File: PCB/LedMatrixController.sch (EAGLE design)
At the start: 31 parts, among them IC2 74LS595D, X1 MINI-USB-32005-201

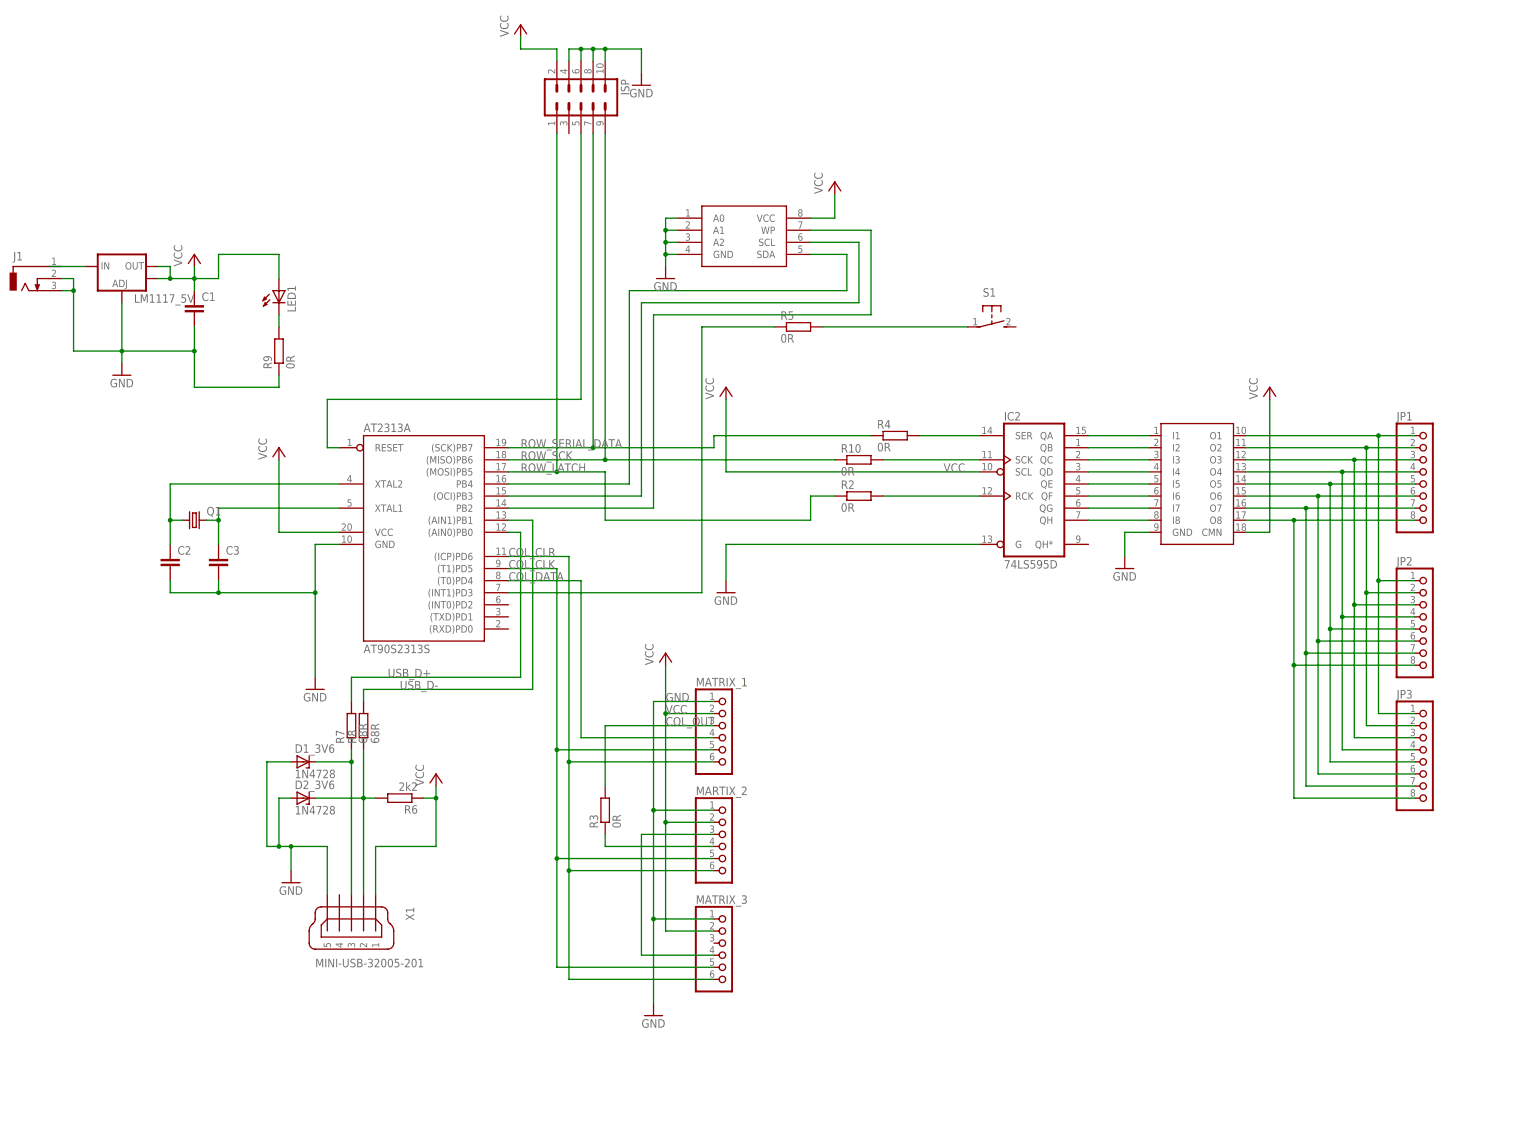
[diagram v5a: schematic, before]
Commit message: Finished first version of the led matrix controller pcb
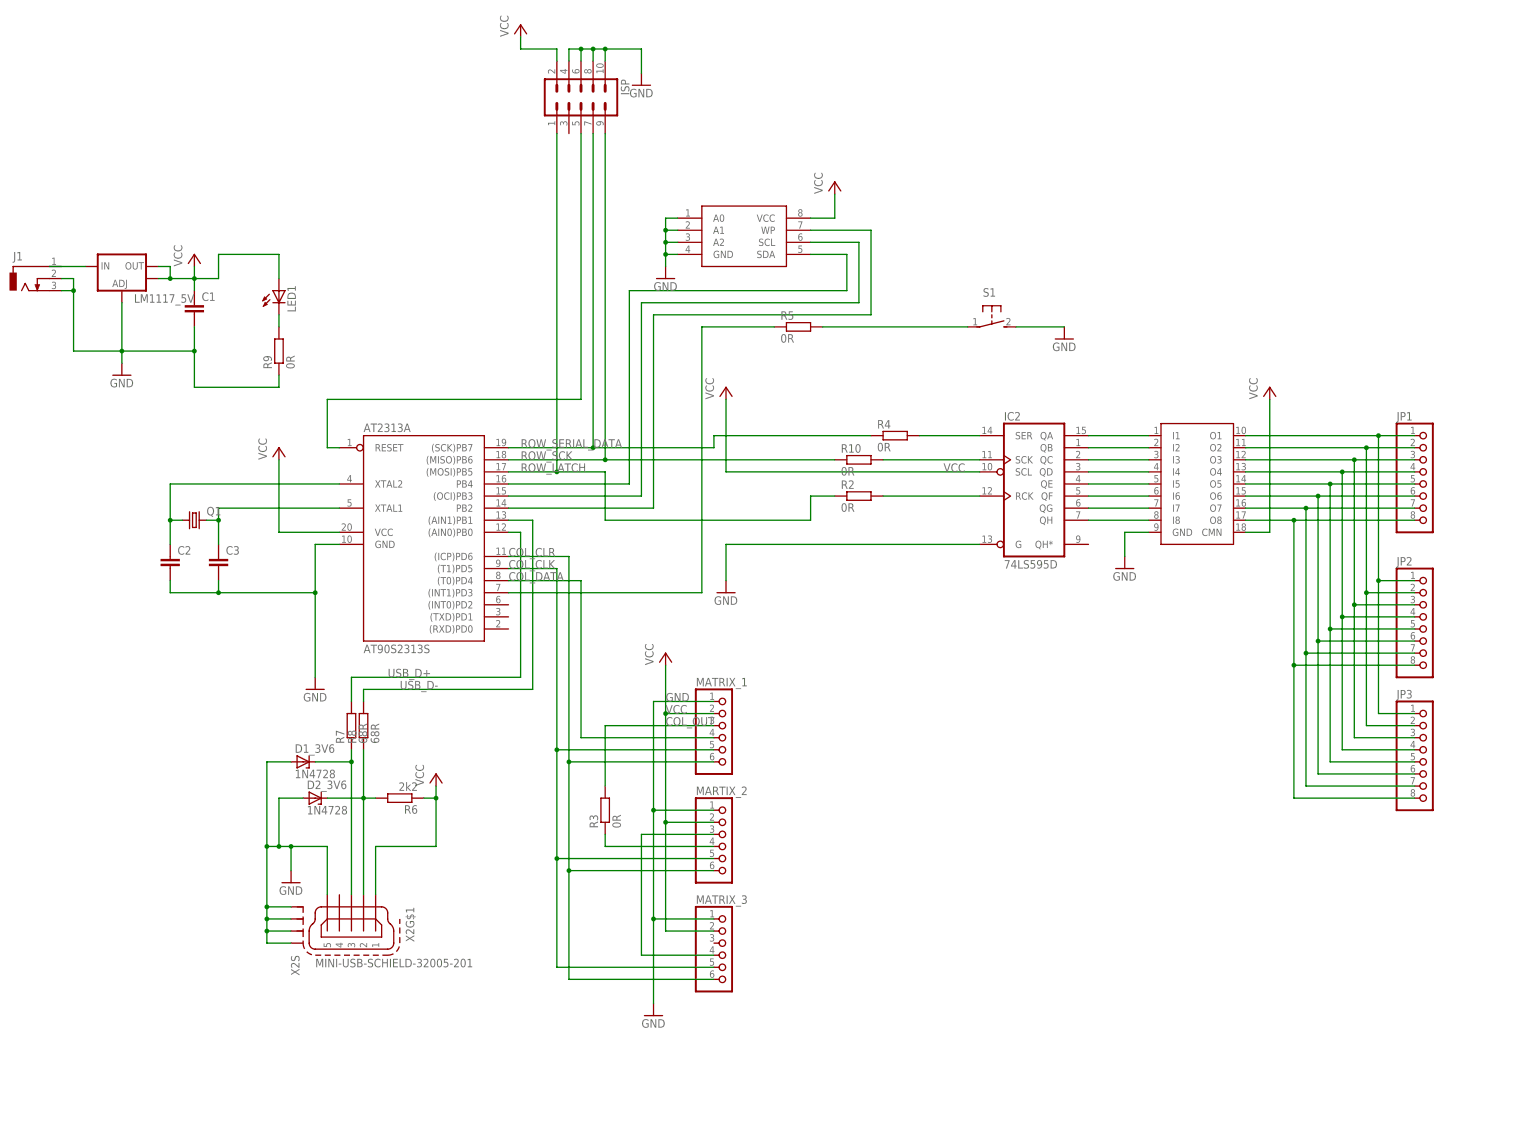
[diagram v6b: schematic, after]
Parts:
- removed X1: MINI-USB-32005-201, con-cypressindustries:MINI-USB-32005-201
- added X2: MINI-USB-SCHIELD-32005-201, con-cypressindustries:MINI-USB-SCHIELD-32005-201
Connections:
- net GND: now also S1.S, X2G$1.5, X2S.S1, X2S.S2, X2S.S3, X2S.S4; no longer X1.5
- net USB_DATA+: now also X2G$1.3; no longer X1.3
- net USB_DATA-: now also X2G$1.2; no longer X1.2
- net VCC: now also X2G$1.1; no longer X1.1
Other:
- moved on the sheet: D2_3V6
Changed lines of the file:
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@@
 <layers>
 <layer number="1" name="Top" color="4" fill="1" visible="no" active="no"/>
-<layer number="16" name="Bottom" color="1" fill="1" visible="no" active="no"/>
+<layer number="16" name="Bottom" color="11" fill="1" visible="no" active="no"/>
 <layer number="17" name="Pads" color="2" fill="1" visible="no" active="no"/>
 <layer number="18" name="Vias" color="2" fill="1" visible="no" active="no"/>
-<layer number="19" name="Unrouted" color="6" fill="1" visible="no" active="no"/>
+<layer number="19" name="Unrouted" color="14" fill="1" visible="no" active="no"/>
 <layer number="20" name="Dimension" color="15" fill="1" visible="no" active="no"/>
 <layer number="21" name="tPlace" color="7" fill="1" visible="no" active="no"/>
@@
 <part name="P+7" library="supply1" deviceset="VCC" device=""/>
 <part name="R5" library="resistor" deviceset="R-EU_" device="R1206" value="0R"/>
-<part name="X1" library="con-cypressindustries" deviceset="MINI-USB-" device="32005-201"/>
 <part name="GND8" library="supply1" deviceset="GND" device=""/>
 <part name="P+8" library="supply1" deviceset="VCC" device=""/>
@@
 <part name="R4" library="resistor" deviceset="R-EU_" device="R1206" value="0R"/>
 <part name="R10" library="resistor" deviceset="R-EU_" device="R1206" value="0R"/>
+<part name="X2" library="con-cypressindustries" deviceset="MINI-USB-SCHIELD-" device="32005-201"/>
+<part name="GND9" library="supply1" deviceset="GND" device=""/>
 </parts>
 <sheets>
@@
 <instance part="P+7" gate="VCC" x="223.52" y="76.2"/>
 <instance part="R5" gate="G$1" x="124.46" y="88.9"/>
-<instance part="X1" gate="G$1" x="30.48" y="-35.56" rot="R270"/>
 <instance part="GND8" gate="1" x="17.78" y="-27.94"/>
 <instance part="P+8" gate="VCC" x="48.26" y="-5.08"/>
@@
 <instance part="R8" gate="G$1" x="33.02" y="5.08" rot="R90"/>
 <instance part="D1_3V6" gate="1" x="20.32" y="-2.54"/>
-<instance part="D2_3V6" gate="1" x="20.32" y="-10.16"/>
+<instance part="D2_3V6" gate="1" x="22.86" y="-10.16"/>
 <instance part="LED1" gate="G$1" x="15.24" y="96.52"/>
 <instance part="R9" gate="G$1" x="15.24" y="83.82" rot="R90"/>
 <instance part="R4" gate="G$1" x="144.78" y="66.04"/>
 <instance part="R10" gate="G$1" x="137.16" y="60.96"/>
+<instance part="X2" gate="G$1" x="30.48" y="-35.56" rot="R270"/>
+<instance part="X2" gate="S" x="20.32" y="-35.56" rot="R270"/>
+<instance part="GND9" gate="1" x="180.34" y="86.36"/>
 </instances>
 <busses>
@@
 <wire x1="17.78" y1="-25.4" x2="17.78" y2="-20.32" width="0.1524" layer="91"/>
 <wire x1="17.78" y1="-20.32" x2="25.4" y2="-20.32" width="0.1524" layer="91"/>
-<pinref part="X1" gate="G$1" pin="5"/>
 <wire x1="25.4" y1="-20.32" x2="25.4" y2="-30.48" width="0.1524" layer="91"/>
 <pinref part="D2_3V6" gate="1" pin="A"/>
-<wire x1="17.78" y1="-10.16" x2="15.24" y2="-10.16" width="0.1524" layer="91"/>
+<wire x1="20.32" y1="-10.16" x2="15.24" y2="-10.16" width="0.1524" layer="91"/>
 <wire x1="15.24" y1="-10.16" x2="15.24" y2="-20.32" width="0.1524" layer="91"/>
 <wire x1="15.24" y1="-20.32" x2="17.78" y2="-20.32" width="0.1524" layer="91"/>
@@
 <junction x="17.78" y="-20.32"/>
 <junction x="15.24" y="-20.32"/>
+<pinref part="X2" gate="G$1" pin="5"/>
+<pinref part="X2" gate="S" pin="S1"/>
+<wire x1="17.78" y1="-33.02" x2="12.7" y2="-33.02" width="0.1524" layer="91"/>
+<wire x1="12.7" y1="-33.02" x2="12.7" y2="-20.32" width="0.1524" layer="91"/>
+<wire x1="12.7" y1="-33.02" x2="12.7" y2="-35.56" width="0.1524" layer="91"/>
+<pinref part="X2" gate="S" pin="S2"/>
+<wire x1="17.78" y1="-35.56" x2="12.7" y2="-35.56" width="0.1524" layer="91"/>
+<wire x1="12.7" y1="-35.56" x2="12.7" y2="-38.1" width="0.1524" layer="91"/>
+<pinref part="X2" gate="S" pin="S3"/>
+<wire x1="17.78" y1="-38.1" x2="12.7" y2="-38.1" width="0.1524" layer="91"/>
+<wire x1="12.7" y1="-38.1" x2="12.7" y2="-40.64" width="0.1524" layer="91"/>
+<pinref part="X2" gate="S" pin="S4"/>
+<wire x1="12.7" y1="-40.64" x2="17.78" y2="-40.64" width="0.1524" layer="91"/>
+<junction x="12.7" y="-38.1"/>
+<junction x="12.7" y="-35.56"/>
+<junction x="12.7" y="-33.02"/>
+<junction x="12.7" y="-20.32"/>
+</segment>
+<segment>
+<pinref part="S1" gate="1" pin="S"/>
+<pinref part="GND9" gate="1" pin="GND"/>
+<wire x1="170.18" y1="88.9" x2="180.34" y2="88.9" width="0.1524" layer="91"/>
 </segment>
 </net>
@@
 </segment>
 <segment>
-<pinref part="X1" gate="G$1" pin="1"/>
 <wire x1="35.56" y1="-30.48" x2="35.56" y2="-20.32" width="0.1524" layer="91"/>
 <wire x1="35.56" y1="-20.32" x2="48.26" y2="-20.32" width="0.1524" layer="91"/>
@@
 <wire x1="45.72" y1="-10.16" x2="48.26" y2="-10.16" width="0.1524" layer="91"/>
 <junction x="48.26" y="-10.16"/>
+<pinref part="X2" gate="G$1" pin="1"/>
 </segment>
 </net>
@@
 <net name="USB_DATA+" class="0">
 <segment>
-<pinref part="X1" gate="G$1" pin="3"/>
 <wire x1="30.48" y1="-30.48" x2="30.48" y2="-2.54" width="0.1524" layer="91"/>
 <pinref part="R7" gate="G$1" pin="1"/>
@@
 <wire x1="22.86" y1="-2.54" x2="30.48" y2="-2.54" width="0.1524" layer="91"/>
 <junction x="30.48" y="-2.54"/>
+<pinref part="X2" gate="G$1" pin="3"/>
 </segment>
 </net>
 <net name="USB_DATA-" class="0">
 <segment>
-<pinref part="X1" gate="G$1" pin="2"/>
 <wire x1="33.02" y1="-30.48" x2="33.02" y2="-10.16" width="0.1524" layer="91"/>
 <pinref part="R8" gate="G$1" pin="1"/>
@@
 <junction x="33.02" y="-10.16"/>
 <pinref part="D2_3V6" gate="1" pin="C"/>
-<wire x1="22.86" y1="-10.16" x2="33.02" y2="-10.16" width="0.1524" layer="91"/>
-</segment>
-</net>
+<wire x1="25.4" y1="-10.16" x2="33.02" y2="-10.16" width="0.1524" layer="91"/>
+<pinref part="X2" gate="G$1" pin="2"/>
+</segment>
+</net>

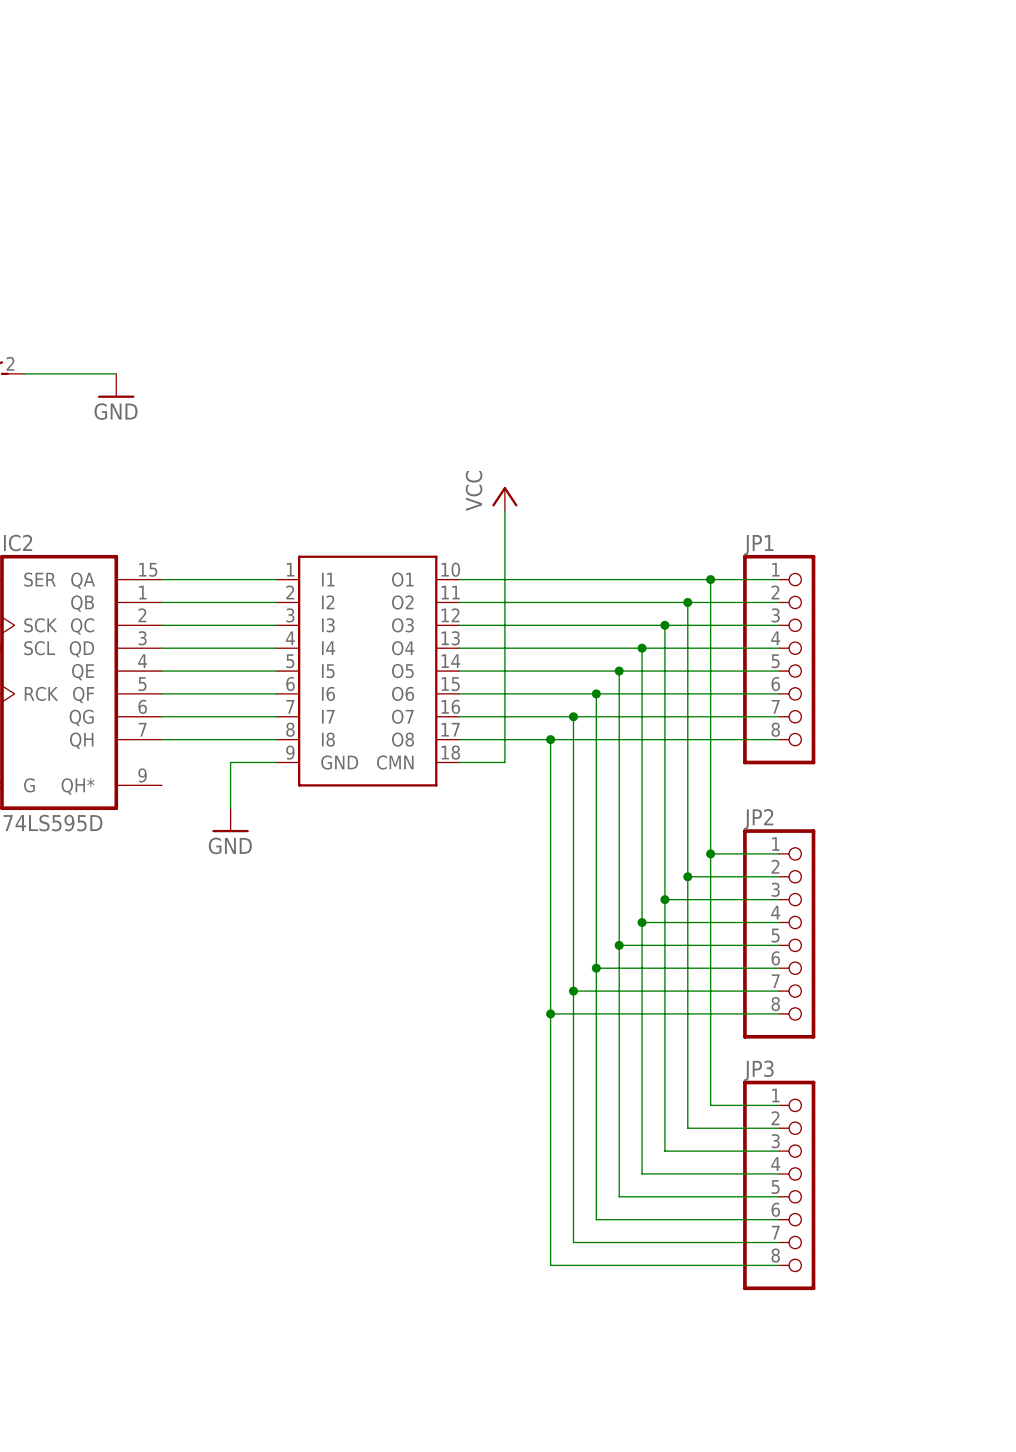
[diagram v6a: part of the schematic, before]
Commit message: ULN2803 has been replaced with NPN transistors
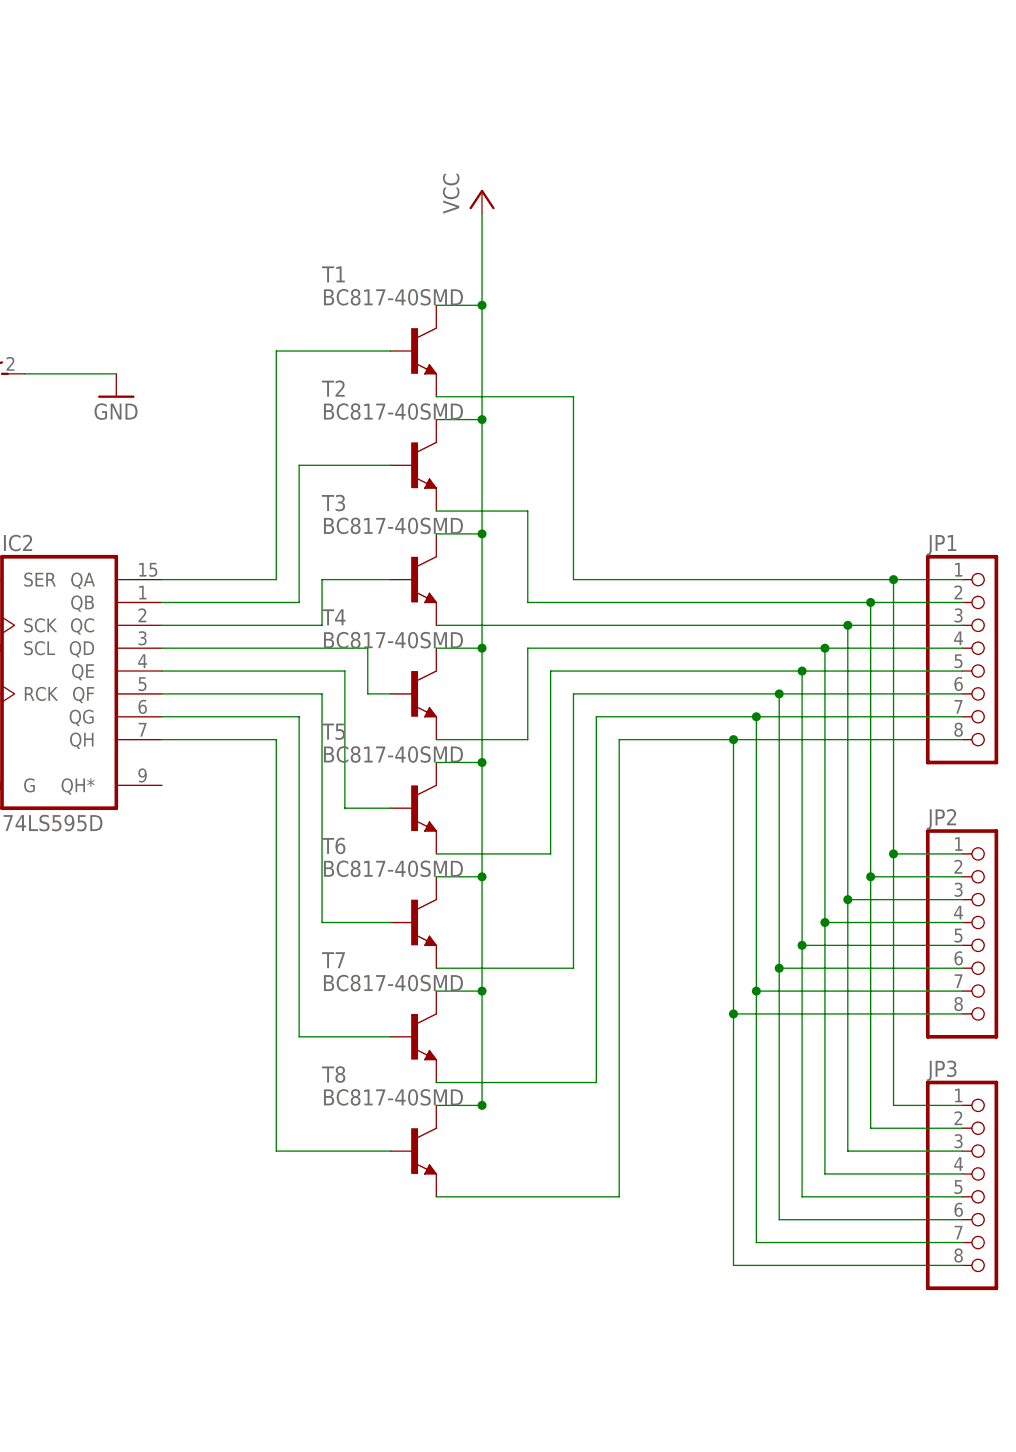
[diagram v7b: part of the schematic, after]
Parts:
- removed U$1: ULN2803A, MJ:ULN2803A
- added T1, T2, T3, T4, T5, T6, T7, T8: BC817-40SMD, transistor-npn:BC817-40SMD
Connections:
- net GND: no longer U$1.GND
- net R1: now also T1.B; no longer U$1.I1
- net R2: now also T2.B; no longer U$1.I2
- net R3: now also T3.B; no longer U$1.I3
- net R4: now also T4.B; no longer U$1.I4
- net R5: now also T5.B; no longer U$1.I5
- net R6: now also T6.B; no longer U$1.I6
- net R7: now also T7.B; no longer U$1.I7
- net R8: now also T8.B; no longer U$1.I8
- net ROW1: now also T1.E; no longer U$1.O1
- net ROW2: now also T2.E; no longer U$1.O2
- net ROW3: now also T3.E; no longer U$1.O3
- net ROW4: now also T4.E; no longer U$1.O4
- net ROW5: now also T5.E; no longer U$1.O5
- net ROW6: now also T6.E; no longer U$1.O6
- net ROW7: now also T7.E; no longer U$1.O7
- net ROW8: now also T8.E; no longer U$1.O8
- net VCC: now also T1.C, T2.C, T3.C, T4.C, T5.C, T6.C, T7.C, T8.C; no longer U$1.CMN
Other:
- moved on the sheet: JP1, JP2, JP3
